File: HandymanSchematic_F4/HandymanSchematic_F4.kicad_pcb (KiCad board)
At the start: 4 copper layers, 53 x 45.5 mm, 79 parts, among them J1 SWD Header, J2 JACKS, J5 ScopeGroundLoop, Q1 BC847, Q2 2N7002, Q3 2N7002, SW1 RST, SW2 BYP, SW302 BOOT, U2 TL074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

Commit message: new prelim routing, DRC passing
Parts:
- removed C2: 10n, Capacitor_SMD:C_0805_2012Metric
- removed SW302: BOOT, Button_Switch_SMD:SW_SPST_B3U-1000P
- C16, C17, TP1, TP2, TP3, U4: moved to B.Cu
- C20: moved to F.Cu
- R310: value 100k -> 10k
- moved R2 46.5 mm to (48.7, 34.1), turned to 0 degrees
- moved R1 44.7 mm to (48.7, 36.2), turned to 0 degrees
- moved C1 43.1 mm to (48.7, 38.2), turned to 0 degrees
- moved R8 37.6 mm to (2.01, 35.8)
- moved D6 37.5 mm to (9.71, 35.9), turned to 0 degrees
- moved R22 37.1 mm to (5.74, 33.2), turned to 0 degrees
- moved R19 37.0 mm to (5.74, 29.8), turned to 0 degrees
- moved U6 36.8 mm to (43.1, 36.3), turned to 0 degrees
- moved C6 36.7 mm to (2.02, 39.3), turned to 90 degrees
- moved SW1 36.2 mm to (50.8, 16.1), turned to 90 degrees
- moved C10 34.8 mm to (12.2, 39.3), turned to 0 degrees
- moved R28 34.5 mm to (37.6, 34.7), turned to 0 degrees
- moved D7 34.4 mm to (14.6, 35.9), turned to 0 degrees
- moved TP2 34.2 mm to (18.9, 35.9), turned to -90 degrees
- moved R24 34.2 mm to (37.6, 32.7), turned to 180 degrees
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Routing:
- net +3.3V: track 266.1 -> 216.8 mm
- net NRST: track 51.3 -> 25.3 mm, vias 4 -> 2
- net Net-(U2D--): track 8.07 -> 31.7 mm
- net Net-(D4-A): track 25.1 -> 1.84 mm
- net /Analog/VG: track 82.2 -> 61.6 mm, vias 4 -> 3
- net SWDIO: track 33.1 -> 12.5 mm, vias 1 -> 0
- net RELEASE_IN: track 24.8 -> 45.0 mm
- net CLOSED_OUT: track 50.3 -> 30.8 mm, vias 1 -> 2
- net /Digital/GateLED: track 28.1 -> 45.8 mm
- net /Digital/GateByp: track 31.6 -> 44.8 mm, vias 2 -> 1
- net SWCLK: track 23.6 -> 11.6 mm, vias 1 -> 0
- net /Digital/BOOT0: track 14.7 -> 2.83 mm
- net FX_IN: track 34.3 -> 23.7 mm, vias 0 -> 1
- net /Digital/TunerModeIn: track 47.8 -> 58.0 mm
- net GND: track 40.8 -> 31.5 mm, vias 75 -> 22
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
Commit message: stitching vias, trace niceties
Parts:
- moved C1 1.37 mm to (48.7, 39.6)
- moved R9 0.24 mm to (23.0, 27.3)
- moved R13 0.22 mm to (16.4, 26.5)
- moved C10 0.08 mm to (12.3, 39.3)
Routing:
- net GND: track 31.5 -> 45.0 mm, vias 22 -> 52
- net +3.3V: track 216.8 -> 219.5 mm
- net /Digital/GateByp: track 44.8 -> 42.7 mm
- net /Analog/VG: track 61.6 -> 63.3 mm
- net /Digital/SCL: track 27.8 -> 28.8 mm
- net Net-(U2C--): track 7.90 -> 7.02 mm
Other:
- board text added: "Rev 2- 03/2026 Hayden Setlik"
- board text removed: "Rev 1- 02/2026 Hayden Setlik"

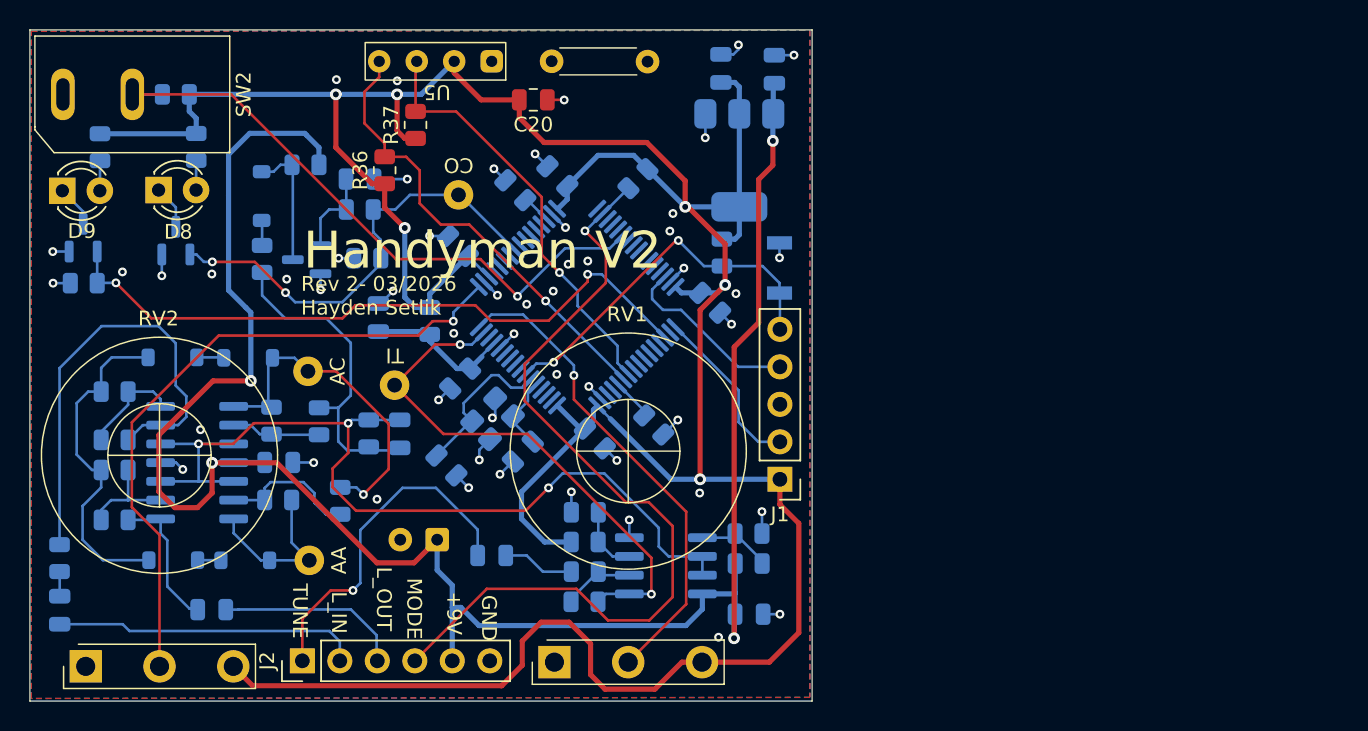
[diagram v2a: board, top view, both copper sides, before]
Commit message: removed acute angles, slikscreen stuff
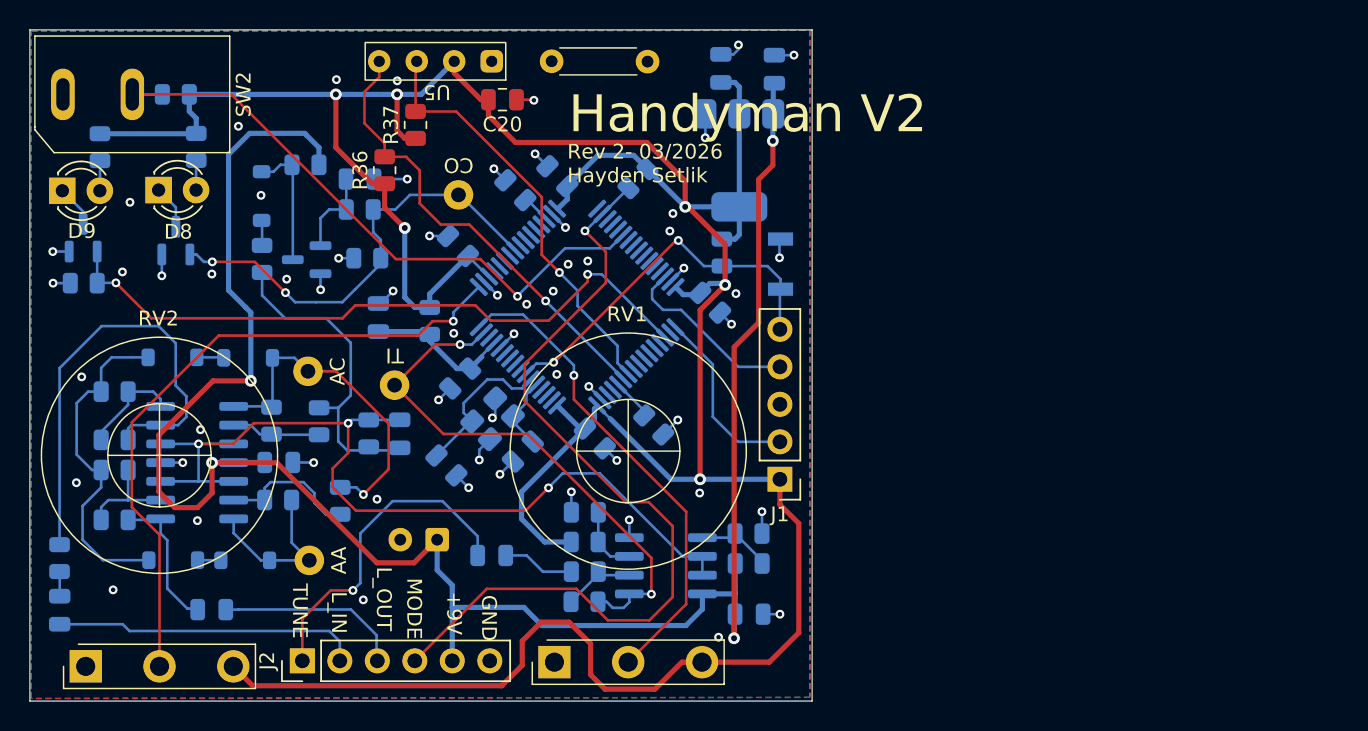
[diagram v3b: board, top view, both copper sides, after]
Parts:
- moved C20 2.09 mm to (32.0, 4.73)
- moved SW1 0.27 mm to (50.9, 15.9)
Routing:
- net FX_IN: track 23.4 -> 22.3 mm
- net SWCLK: track 11.6 -> 12.4 mm
- net /Analog/VG: track 63.3 -> 62.6 mm
- net TUNE_IN: track 36.1 -> 36.8 mm
- net GND: track 45.0 -> 45.2 mm, vias 52 -> 60

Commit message: minor nudges for rev2
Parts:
- moved R12 0.46 mm to (5.29, 27.9)
- moved R19 0.46 mm to (5.29, 29.9)
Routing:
- net /Analog/VG: track 62.6 -> 65.6 mm
- net GND: track 45.2 -> 42.7 mm, vias 60 -> 61
